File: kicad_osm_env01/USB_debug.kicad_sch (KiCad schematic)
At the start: 22 parts

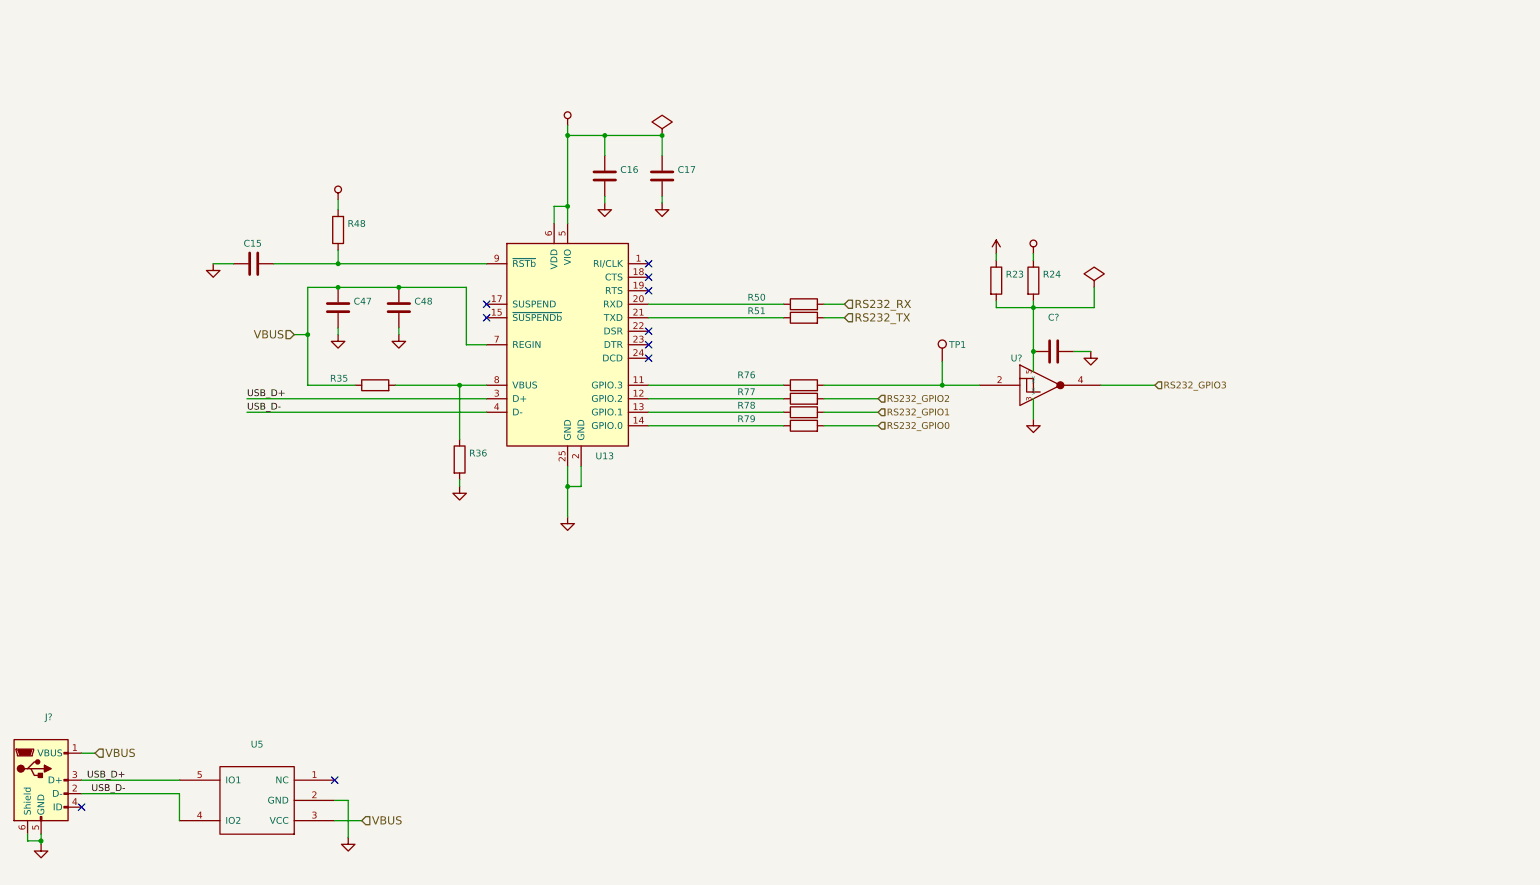
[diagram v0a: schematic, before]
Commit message: added stml433 to schematic and carried out some mods
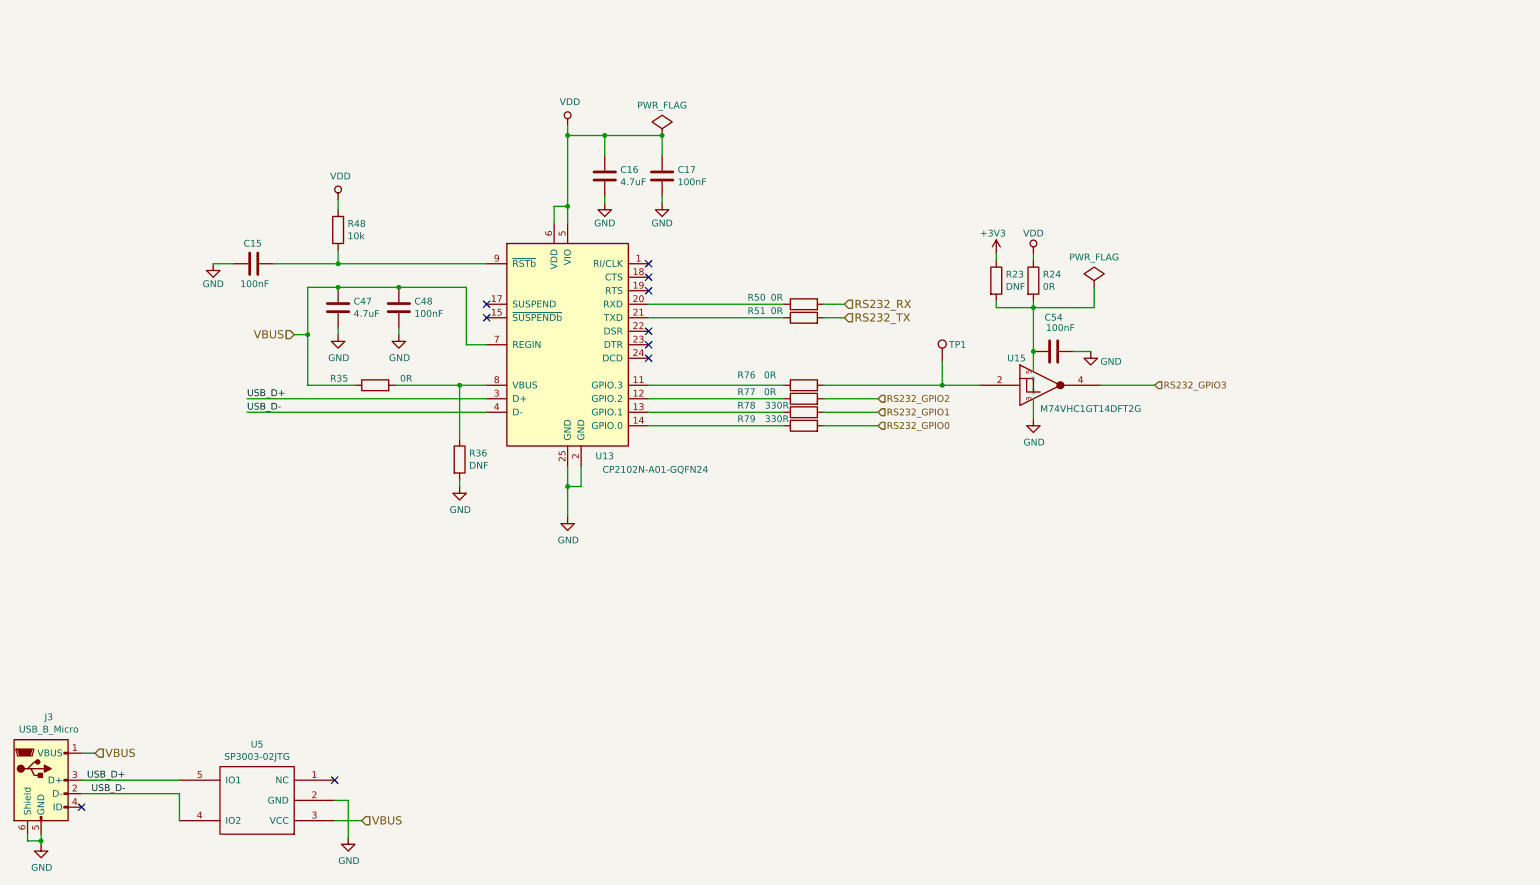
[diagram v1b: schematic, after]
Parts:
- C15, C17, C48: value (none) -> 100nF; footprint (none) -> Capacitor_SMD:C_0402_1005Metric
- C16, C47: value (none) -> 4.7uF; footprint (none) -> Capacitor_SMD:C_0603_1608Metric
- C54: renamed from C?; value (none) -> 100nF; footprint (none) -> Capacitor_SMD:C_0402_1005Metric
- J3: renamed from J?; value (none) -> USB_B_Micro; footprint (none) -> Devtank_PCB_lib:MOLEX_105017-0001_USB_B
- R23, R36: value (none) -> DNF; footprint (none) -> Resistor_SMD:R_0603_1608Metric
- R24, R35, R50, R51, R76, R77: value (none) -> 0R; footprint (none) -> Resistor_SMD:R_0603_1608Metric
- R48: value (none) -> 10k; footprint (none) -> Resistor_SMD:R_0603_1608Metric
- R78, R79: value (none) -> 330R; footprint (none) -> Resistor_SMD:R_0603_1608Metric
- TP1: value (none) -> Test_Point; footprint (none) -> TestPoint:TestPoint_Pad_D1.5mm
- U13: value (none) -> CP2102N-A01-GQFN24; footprint (none) -> Devtank_PCB_lib:CP2102_QFN-24-1EP_4x4mm_P0.5mm_EP2.6x2.6mm_ThermalVias_0.3mmdrill
- U15: renamed from U?; value (none) -> M74VHC1GT14DFT2G; footprint (none) -> Package_TO_SOT_SMD:SOT-353_SC-70-5
- U5: value (none) -> SP3003-02JTG; footprint (none) -> Package_TO_SOT_SMD:SOT-353_SC-70-5

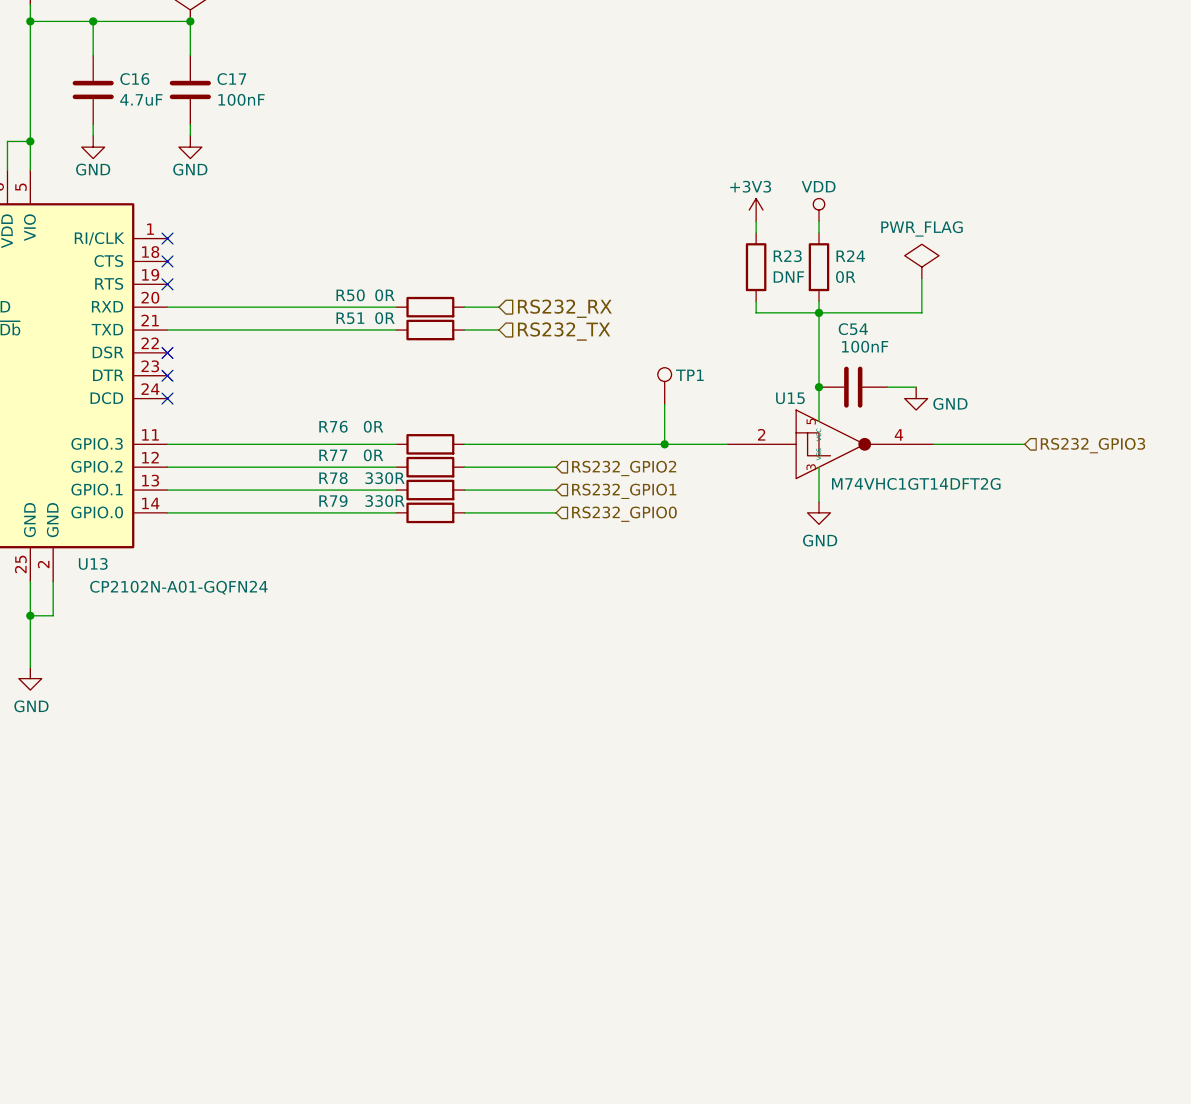
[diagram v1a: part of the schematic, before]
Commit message: updated schematics
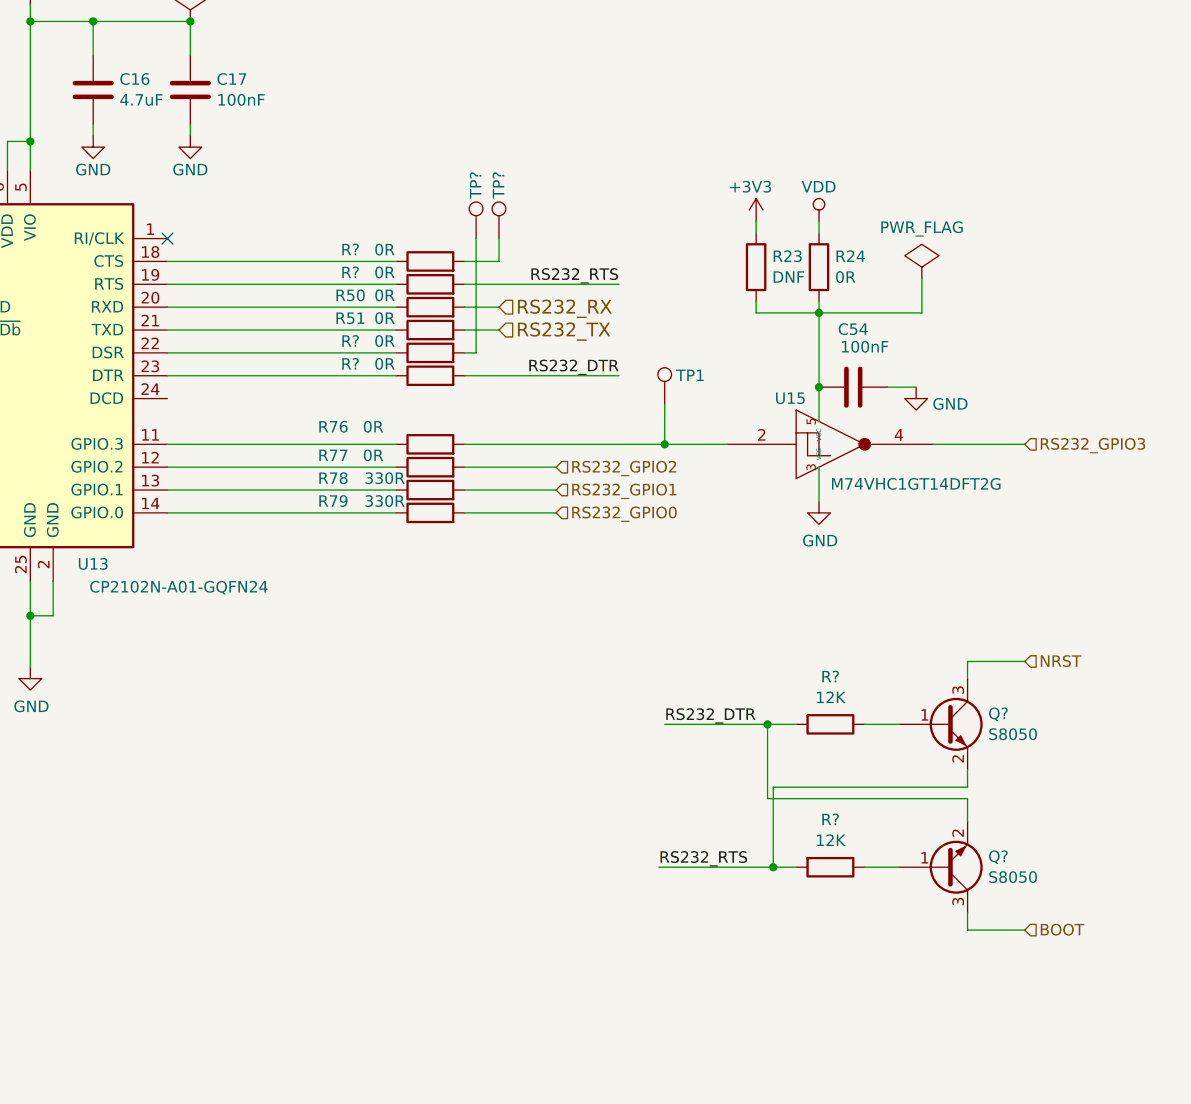
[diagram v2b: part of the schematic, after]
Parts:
- added Q? (x2): S8050, Package_TO_SOT_SMD:SOT-23, symbol device:Q_NPN_BEC
- added R? (x2): 12K, Resistor_SMD:R_0603_1608Metric, symbol device:R
- added R? (x4): 0R, Resistor_SMD:R_0603_1608Metric, symbol OSM_env01-rescue:R-device-ESP32-EVB_Rev_D-rescue
- added TP? (x2): Test_Point, TestPoint:TestPoint_Pad_D1.5mm, symbol Connector:Test_Point
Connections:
- net at U13.18 (CTS): now also R?.1
- net at U13.19 (RTS): now also R?.1
- net at U13.22 (DSR): now also R?.1
- net at U13.23 (DTR): now also R?.1
- new net: Q?.1 (B), R?.1 (x2)
- new net: R?.2, TP?.1 (x2)
- new net BOOT: Q?.3 (C)
- new net NRST: Q?.3 (C)
- new net RS232_DTR: Q?.2 (E), R?.2, R?.2
- new net RS232_RTS: Q?.2 (E), R?.2, R?.2
- no-connect marks 10 -> 5

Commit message: added new battery charge ic u2
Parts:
- gave numbers to parts that had none: 10
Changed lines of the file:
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@@
   (title_block
     (title "Open Smart Monitor")
-    (date "2021-09-29")
-    (rev "B")
+    (date "2022-07-01")
+    (rev "C")
     (company "Devtank LTD")
     (comment 1 "Part No: 304-010")
@@
   (symbol (lib_id "device:R") (at 213.995 142.875 270) (unit 1)
     (in_bom yes) (on_board yes)
-    (property "Reference" "R?" (id 0) (at 213.995 137.6172 90))
+    (property "Reference" "R89" (id 0) (at 213.995 137.6172 90))
     (property "Value" "12K" (id 1) (at 213.995 139.9286 90))
     (property "Footprint" "Resistor_SMD:R_0603_1608Metric" (id 2) (at 213.995 141.097 90)
@@
   (symbol (lib_id "Connector:Test_Point") (at 174.625 73.025 0) (unit 1)
     (in_bom yes) (on_board yes)
-    (property "Reference" "TP?" (id 0) (at 174.625 68.58 90)
+    (property "Reference" "TP59" (id 0) (at 174.625 68.58 90)
       (effects (font (size 1.27 1.27)) (justify left))
     )
@@
   (symbol (lib_id "OSM_env01-rescue:R-device-ESP32-EVB_Rev_D-rescue") (at 169.545 85.725 90) (unit 1)
     (in_bom yes) (on_board yes)
-    (property "Reference" "R?" (id 0) (at 160.655 84.455 90))
+    (property "Reference" "R81" (id 0) (at 160.655 84.455 90))
     (property "Value" "0R" (id 1) (at 164.465 84.455 90))
     (property "Footprint" "Resistor_SMD:R_0603_1608Metric" (id 2) (at 169.545 87.503 90)
@@
   (symbol (lib_id "OSM_env01-rescue:R-device-ESP32-EVB_Rev_D-rescue") (at 169.545 88.265 90) (unit 1)
     (in_bom yes) (on_board yes)
-    (property "Reference" "R?" (id 0) (at 160.655 86.995 90))
+    (property "Reference" "R82" (id 0) (at 160.655 86.995 90))
     (property "Value" "0R" (id 1) (at 164.465 86.995 90))
     (property "Footprint" "Resistor_SMD:R_0603_1608Metric" (id 2) (at 169.545 90.043 90)
@@
   (symbol (lib_id "device:Q_NPN_BEC") (at 226.695 142.875 0) (mirror x) (unit 1)
     (in_bom yes) (on_board yes)
-    (property "Reference" "Q?" (id 0) (at 231.521 141.7066 0)
+    (property "Reference" "Q3" (id 0) (at 231.521 141.7066 0)
       (effects (font (size 1.27 1.27)) (justify left))
     )
@@
   (symbol (lib_id "OSM_env01-rescue:R-device-ESP32-EVB_Rev_D-rescue") (at 169.545 75.565 90) (unit 1)
     (in_bom yes) (on_board yes)
-    (property "Reference" "R?" (id 0) (at 160.655 74.295 90))
+    (property "Reference" "R71" (id 0) (at 160.655 74.295 90))
     (property "Value" "0R" (id 1) (at 164.465 74.295 90))
     (property "Footprint" "Resistor_SMD:R_0603_1608Metric" (id 2) (at 169.545 77.343 90)
@@
   (symbol (lib_id "Connector:Test_Point") (at 177.165 73.025 0) (unit 1)
     (in_bom yes) (on_board yes)
-    (property "Reference" "TP?" (id 0) (at 177.165 68.58 90)
+    (property "Reference" "TP60" (id 0) (at 177.165 68.58 90)
       (effects (font (size 1.27 1.27)) (justify left))
     )
@@
   (symbol (lib_id "device:R") (at 213.995 127 270) (unit 1)
     (in_bom yes) (on_board yes)
-    (property "Reference" "R?" (id 0) (at 213.995 121.7422 90))
+    (property "Reference" "R86" (id 0) (at 213.995 121.7422 90))
     (property "Value" "12K" (id 1) (at 213.995 124.0536 90))
     (property "Footprint" "Resistor_SMD:R_0603_1608Metric" (id 2) (at 213.995 125.222 90)
@@
   (symbol (lib_id "device:Q_NPN_BEC") (at 226.695 127 0) (unit 1)
     (in_bom yes) (on_board yes)
-    (property "Reference" "Q?" (id 0) (at 231.521 125.8316 0)
+    (property "Reference" "Q2" (id 0) (at 231.521 125.8316 0)
       (effects (font (size 1.27 1.27)) (justify left))
     )
@@
   (symbol (lib_id "OSM_env01-rescue:R-device-ESP32-EVB_Rev_D-rescue") (at 169.545 78.105 90) (unit 1)
     (in_bom yes) (on_board yes)
-    (property "Reference" "R?" (id 0) (at 160.655 76.835 90))
+    (property "Reference" "R80" (id 0) (at 160.655 76.835 90))
     (property "Value" "0R" (id 1) (at 164.465 76.835 90))
     (property "Footprint" "Resistor_SMD:R_0603_1608Metric" (id 2) (at 169.545 79.883 90)

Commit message: updated schematics and added rs232
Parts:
- added R130: 0R, Resistor_SMD:R_0603_1608Metric, symbol OSM_env01-rescue:R-device-ESP32-EVB_Rev_D-rescue
- added TP24, TP62, TP63: Test_Point, TestPoint:TestPoint_Pad_D1.5mm, symbol Connector:Test_Point
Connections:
- net RS232_DTR: now also TP63.1
- net RS232_RTS: now also TP62.1
- net at U13.24 (DCD): now also R130.1
- new net: R130.2, TP24.1
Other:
- moved on the sheet: TP59
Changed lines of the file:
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@@
+    (stroke (width 0) (type default) (color 0 0 0 0))
+  )
+  (wire (pts (xy 173.99 73.025) (xy 173.355 73.025))
     (stroke (width 0) (type default) (color 0 0 0 0))
   )
@@
     (stroke (width 0) (type default) (color 0 0 0 0))
   )
-  (wire (pts (xy 174.625 73.025) (xy 174.625 85.725))
+  (wire (pts (xy 175.26 73.025) (xy 175.26 85.725))
     (stroke (width 0) (type default) (color 0 0 0 0))
   )
@@
     (stroke (width 0) (type default) (color 0 0 0 0))
   )
+  (wire (pts (xy 173.99 90.805) (xy 173.99 73.025))
+    (stroke (width 0) (type default) (color 0 0 0 0))
+  )
+  (wire (pts (xy 173.355 90.805) (xy 173.99 90.805))
+    (stroke (width 0) (type default) (color 0 0 0 0))
+  )
   (wire (pts (xy 229.235 133.985) (xy 207.645 133.985))
     (stroke (width 0) (type default) (color 0 0 0 0))
@@
     (stroke (width 0) (type default) (color 0 0 0 0))
   )
-  (wire (pts (xy 174.625 85.725) (xy 173.355 85.725))
+  (wire (pts (xy 175.26 85.725) (xy 173.355 85.725))
     (stroke (width 0) (type default) (color 0 0 0 0))
   )
@@
   )
   (wire (pts (xy 33.655 172.72) (xy 52.07 172.72))
+    (stroke (width 0) (type default) (color 0 0 0 0))
+  )
+  (wire (pts (xy 140.335 90.805) (xy 165.735 90.805))
     (stroke (width 0) (type default) (color 0 0 0 0))
   )
@@
     (pin "1")
   )
+  (symbol (lib_id "OSM_env01-rescue:R-device-ESP32-EVB_Rev_D-rescue") (at 169.545 90.805 90) (unit 1)
+    (in_bom yes) (on_board yes)
+    (property "Reference" "R130" (id 0) (at 160.655 89.535 90))
+    (property "Value" "0R" (id 1) (at 164.465 89.535 90))
+    (property "Footprint" "Resistor_SMD:R_0603_1608Metric" (id 2) (at 169.545 92.583 90)
+      (effects (font (size 1.27 1.27)) hide)
+    )
+    (property "Datasheet" "" (id 3) (at 169.545 90.805 0)
+      (effects (font (size 1.27 1.27)) hide)
+    )
+    (pin "1")
+    (pin "2")
+  )
   (symbol (lib_id "device:R") (at 213.995 142.875 270) (unit 1)
     (in_bom yes) (on_board yes)
@@
     (pin "2")
   )
-  (symbol (lib_id "Connector:Test_Point") (at 174.625 73.025 0) (unit 1)
-    (in_bom yes) (on_board yes)
-    (property "Reference" "TP59" (id 0) (at 174.625 68.58 90)
-      (effects (font (size 1.27 1.27)) (justify left))
-    )
-    (property "Value" "Test_Point" (id 1) (at 176.0982 72.3392 0)
+  (symbol (lib_id "Connector:Test_Point") (at 175.26 73.025 0) (unit 1)
+    (in_bom yes) (on_board yes)
+    (property "Reference" "TP59" (id 0) (at 175.26 68.58 90)
+      (effects (font (size 1.27 1.27)) (justify left))
+    )
+    (property "Value" "Test_Point" (id 1) (at 176.7332 72.3392 0)
       (effects (font (size 1.27 1.27)) (justify left) hide)
     )
-    (property "Footprint" "TestPoint:TestPoint_Pad_D1.5mm" (id 2) (at 179.705 73.025 0)
-      (effects (font (size 1.27 1.27)) hide)
-    )
-    (property "Datasheet" "~" (id 3) (at 179.705 73.025 0)
+    (property "Footprint" "TestPoint:TestPoint_Pad_D1.5mm" (id 2) (at 180.34 73.025 0)
+      (effects (font (size 1.27 1.27)) hide)
+    )
+    (property "Datasheet" "~" (id 3) (at 180.34 73.025 0)
       (effects (font (size 1.27 1.27)) hide)
     )
@@
     (pin "3")
   )
+  (symbol (lib_id "Connector:Test_Point") (at 173.355 73.025 0) (unit 1)
+    (in_bom yes) (on_board yes)
+    (property "Reference" "TP24" (id 0) (at 173.355 68.58 90)
+      (effects (font (size 1.27 1.27)) (justify left))
+    )
+    (property "Value" "Test_Point" (id 1) (at 174.8282 72.3392 0)
+      (effects (font (size 1.27 1.27)) (justify left) hide)
+    )
+    (property "Footprint" "TestPoint:TestPoint_Pad_D1.5mm" (id 2) (at 178.435 73.025 0)
+      (effects (font (size 1.27 1.27)) hide)
+    )
+    (property "Datasheet" "~" (id 3) (at 178.435 73.025 0)
+      (effects (font (size 1.27 1.27)) hide)
+    )
+    (pin "1")
+  )
+  (symbol (lib_id "Connector:Test_Point") (at 190.5 78.105 270) (unit 1)
+    (in_bom yes) (on_board yes)
+    (property "Reference" "TP62" (id 0) (at 194.945 78.105 90)
+      (effects (font (size 1.27 1.27)) (justify left))
+    )
+    (property "Value" "Test_Point" (id 1) (at 191.1858 79.5782 0)
+      (effects (font (size 1.27 1.27)) (justify left) hide)
+    )
+    (property "Footprint" "TestPoint:TestPoint_Pad_D1.5mm" (id 2) (at 190.5 83.185 0)
+      (effects (font (size 1.27 1.27)) hide)
+    )
+    (property "Datasheet" "~" (id 3) (at 190.5 83.185 0)
+      (effects (font (size 1.27 1.27)) hide)
+    )
+    (pin "1")
+  )
   (symbol (lib_id "OSM_env01-rescue:R-device-ESP32-EVB_Rev_D-rescue") (at 169.545 75.565 90) (unit 1)
     (in_bom yes) (on_board yes)
@@
     (pin "2")
   )
+  (symbol (lib_id "Connector:Test_Point") (at 190.5 88.265 270) (unit 1)
+    (in_bom yes) (on_board yes)
+    (property "Reference" "TP63" (id 0) (at 194.945 88.265 90)
+      (effects (font (size 1.27 1.27)) (justify left))
+    )
+    (property "Value" "Test_Point" (id 1) (at 191.1858 89.7382 0)
+      (effects (font (size 1.27 1.27)) (justify left) hide)
+    )
+    (property "Footprint" "TestPoint:TestPoint_Pad_D1.5mm" (id 2) (at 190.5 93.345 0)
+      (effects (font (size 1.27 1.27)) hide)
+    )
+    (property "Datasheet" "~" (id 3) (at 190.5 93.345 0)
+      (effects (font (size 1.27 1.27)) hide)
+    )
+    (pin "1")
+  )
   (symbol (lib_id "Connector:Test_Point") (at 177.165 73.025 0) (unit 1)
